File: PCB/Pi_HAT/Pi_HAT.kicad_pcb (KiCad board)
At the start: 2 copper layers, 59 x 65 mm, 15 parts, among them J1 MPU9250, J2 Pi_GPIO, J3 Display, J4 Solenoid I2C, J5 Power Supply

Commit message: Added logo
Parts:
- added G***: LOGO, .pretty:eppl_logo, B.Cu at (137.6, 90.9)
- added G***: LOGO, .pretty:eppl_logo, F.Cu at (103.0, 115.6)
- added H5: MountingHole, MountingHole:MountingHole_2.5mm, F.Cu at (142.9, 109.5)
- added H6: MountingHole, MountingHole:MountingHole_2.5mm, F.Cu at (143.5, 130.0)
- J2: value Pi_GPIO -> PI GPIO
- TB1: value ARDUINO_NANO -> ARDUINO NANO
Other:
- board text added: "12V"
- board text added: "3.3V"
- board text added: "GND"
- board text added: "PI HAT EASY CONTROLS"
- board text added: "SCL"
- board text added: "SDA"
- board text removed: "EPPL"
- board text removed: "Raspberry Pi HAT EASY CONTROLS"

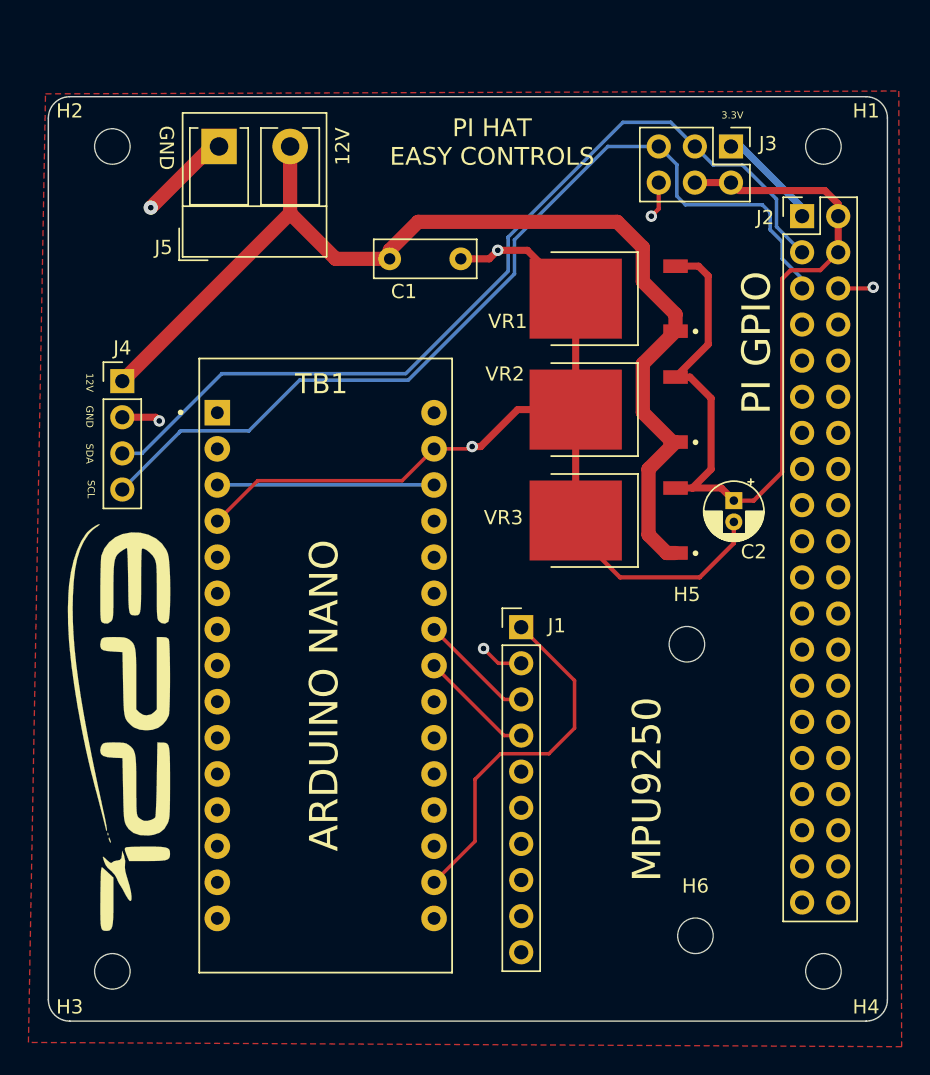
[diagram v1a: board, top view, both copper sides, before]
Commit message: Changed Footprints
Changed the regulator's footprint and added XT-60
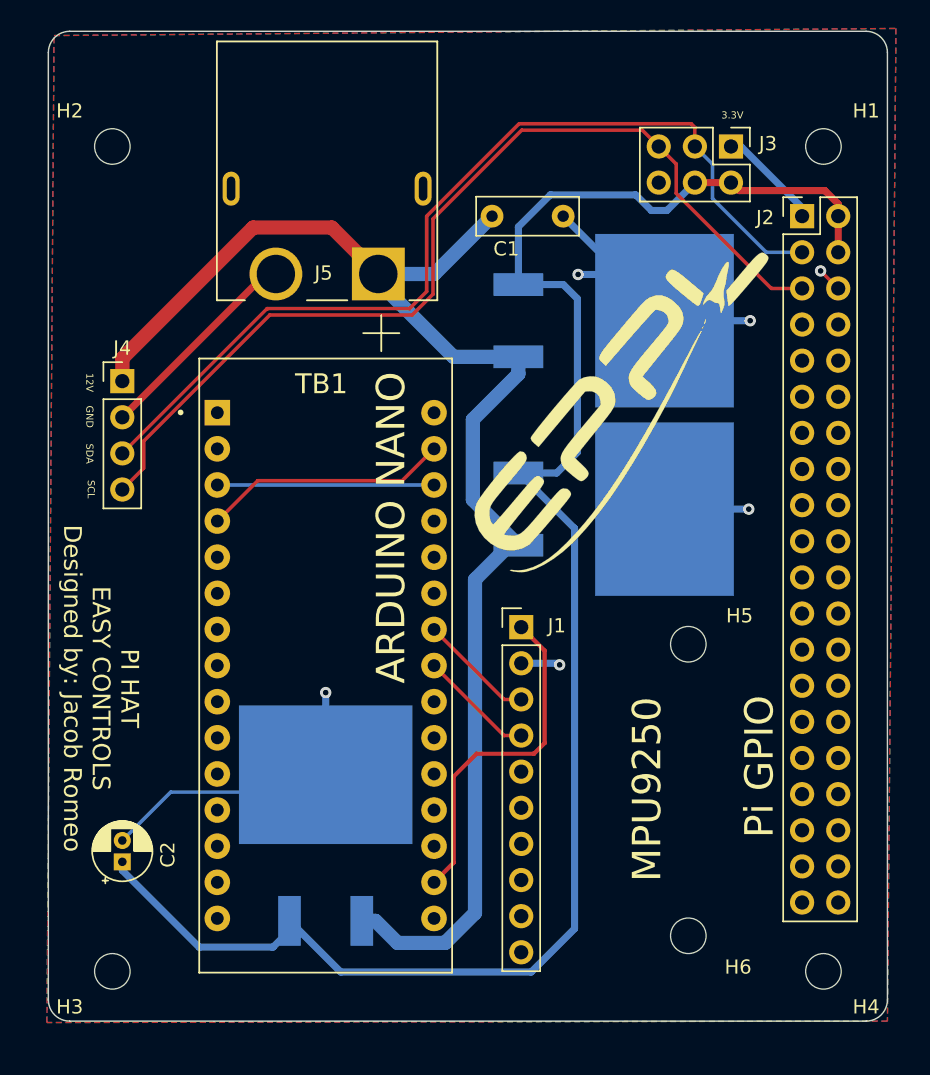
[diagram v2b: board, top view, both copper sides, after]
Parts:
- removed the G*** at (137.6, 90.9)
- removed the G*** at (103.0, 115.6)
- added G***: LOGO, .pretty:eppl_logo, F.Cu at (138.7, 92.3)
- C2: value CP -> C_Polarized
- J2: value PI GPIO -> Pi GPIO
- J5: value Power Supply -> XT60PW-M; footprint TerminalBlock_RND:TerminalBlock_RND_205-00276_1x02_P5.00mm_Vertical -> .pretty:AMASS_XT60PW-M
- VR1, VR2, VR3: value LM78M05CDTX_NOPB -> LM78M05CDTX/NOPB; footprint .pretty:TO228P991X255-3N -> .pretty:VREG_L7805ACD2T; moved to B.Cu
- moved C2 49.9 mm to (103.2, 124.8), turned to 90 degrees
- moved VR3 29.3 mm to (117.5, 122.2), turned to 90 degrees
- moved J5 8.16 mm to (117.6, 77.5)
- moved C1 7.80 mm to (129.2, 79.4)
- moved VR2 7.01 mm to (137.8, 100.0), turned to 0 degrees
- moved VR1 1.59 mm to (137.8, 86.8), turned to 0 degrees
- moved H6 0.50 mm to (143.0, 130.0)
- moved H5 0.10 mm to (143.0, 109.5)
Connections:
- J1 pad 10: Net-(J1-Pad10) -> unconnected-(J1-Pad10)
- J1 pad 5: Net-(J1-Pad5) -> unconnected-(J1-Pad5)
- J1 pad 6: Net-(J1-Pad6) -> unconnected-(J1-Pad6)
- J1 pad 7: Net-(J1-Pad7) -> unconnected-(J1-Pad7)
- J1 pad 8: Net-(J1-Pad8) -> unconnected-(J1-Pad8)
- J1 pad 9: Net-(J1-Pad9) -> unconnected-(J1-Pad9)
- J2 pad 10: Net-(J2-Pad10) -> unconnected-(J2-Pad10)
- J2 pad 11: Net-(J2-Pad11) -> unconnected-(J2-Pad11)
- J2 pad 12: Net-(J2-Pad12) -> unconnected-(J2-Pad12)
- J2 pad 13: Net-(J2-Pad13) -> unconnected-(J2-Pad13)
- J2 pad 14: Net-(J2-Pad14) -> unconnected-(J2-Pad14)
- J2 pad 15: Net-(J2-Pad15) -> unconnected-(J2-Pad15)
- J2 pad 16: Net-(J2-Pad16) -> unconnected-(J2-Pad16)
- J2 pad 17: Net-(J2-Pad17) -> unconnected-(J2-Pad17)
- J2 pad 18: Net-(J2-Pad18) -> unconnected-(J2-Pad18)
- J2 pad 19: Net-(J2-Pad19) -> unconnected-(J2-Pad19)
- J2 pad 20: Net-(J2-Pad20) -> unconnected-(J2-Pad20)
- J2 pad 21: Net-(J2-Pad21) -> unconnected-(J2-Pad21)
- J2 pad 22: Net-(J2-Pad22) -> unconnected-(J2-Pad22)
- J2 pad 23: Net-(J2-Pad23) -> unconnected-(J2-Pad23)
- J2 pad 24: Net-(J2-Pad24) -> unconnected-(J2-Pad24)
- J2 pad 25: Net-(J2-Pad25) -> unconnected-(J2-Pad25)
- J2 pad 26: Net-(J2-Pad26) -> unconnected-(J2-Pad26)
- J2 pad 27: Net-(J2-Pad27) -> unconnected-(J2-Pad27)
- J2 pad 28: Net-(J2-Pad28) -> unconnected-(J2-Pad28)
- J2 pad 29: Net-(J2-Pad29) -> unconnected-(J2-Pad29)
- J2 pad 30: Net-(J2-Pad30) -> unconnected-(J2-Pad30)
- J2 pad 31: Net-(J2-Pad31) -> unconnected-(J2-Pad31)
- J2 pad 32: Net-(J2-Pad32) -> unconnected-(J2-Pad32)
- J2 pad 33: Net-(J2-Pad33) -> unconnected-(J2-Pad33)
- J2 pad 34: Net-(J2-Pad34) -> unconnected-(J2-Pad34)
- J2 pad 35: Net-(J2-Pad35) -> unconnected-(J2-Pad35)
- J2 pad 36: Net-(J2-Pad36) -> unconnected-(J2-Pad36)
- J2 pad 37: Net-(J2-Pad37) -> unconnected-(J2-Pad37)
- J2 pad 38: Net-(J2-Pad38) -> unconnected-(J2-Pad38)
- J2 pad 39: Net-(J2-Pad39) -> unconnected-(J2-Pad39)
- J2 pad 40: Net-(J2-Pad40) -> unconnected-(J2-Pad40)
- J2 pad 7: Net-(J2-Pad7) -> unconnected-(J2-Pad7)
- J2 pad 8: Net-(J2-Pad8) -> unconnected-(J2-Pad8)
- J2 pad 9: Net-(J2-Pad9) -> unconnected-(J2-Pad9)
- J5 pad 1: GND -> 12V
- J5 pad 2: 12V -> GND
- TB1 pad 1: Net-(TB1-Pad1) -> unconnected-(TB1-Pad1)
- TB1 pad 10: Net-(TB1-Pad10) -> unconnected-(TB1-Pad10)
- TB1 pad 11: Net-(TB1-Pad11) -> unconnected-(TB1-Pad11)
- TB1 pad 12: Net-(TB1-Pad12) -> unconnected-(TB1-Pad12)
- TB1 pad 13: Net-(TB1-Pad13) -> unconnected-(TB1-Pad13)
- TB1 pad 14: Net-(TB1-Pad14) -> unconnected-(TB1-Pad14)
- TB1 pad 15: Net-(TB1-Pad15) -> unconnected-(TB1-Pad15)
- TB1 pad 16: Net-(TB1-Pad16) -> unconnected-(TB1-Pad16)
- TB1 pad 18: Net-(TB1-Pad18) -> unconnected-(TB1-Pad18)
- TB1 pad 19: Net-(TB1-Pad19) -> unconnected-(TB1-Pad19)
- TB1 pad 2: Net-(TB1-Pad2) -> unconnected-(TB1-Pad2)
- TB1 pad 20: Net-(TB1-Pad20) -> unconnected-(TB1-Pad20)
- TB1 pad 21: Net-(TB1-Pad21) -> unconnected-(TB1-Pad21)
- TB1 pad 22: Net-(TB1-Pad22) -> unconnected-(TB1-Pad22)
- TB1 pad 25: Net-(TB1-Pad25) -> unconnected-(TB1-Pad25)
- TB1 pad 26: Net-(TB1-Pad26) -> unconnected-(TB1-Pad26)
- TB1 pad 27: Net-(TB1-Pad27) -> unconnected-(TB1-Pad27)
- TB1 pad 28: Net-(TB1-Pad28) -> unconnected-(TB1-Pad28)
- TB1 pad 3: Net-(TB1-Pad28) -> unconnected-(TB1-Pad28)
- TB1 pad 30: Net-(TB1-Pad30) -> unconnected-(TB1-Pad30)
- TB1 pad 5: Net-(TB1-Pad5) -> unconnected-(TB1-Pad5)
- TB1 pad 6: Net-(TB1-Pad6) -> unconnected-(TB1-Pad6)
- TB1 pad 7: Net-(TB1-Pad7) -> unconnected-(TB1-Pad7)
- TB1 pad 8: Net-(TB1-Pad8) -> unconnected-(TB1-Pad8)
- TB1 pad 9: Net-(TB1-Pad9) -> unconnected-(TB1-Pad9)
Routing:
- net /5V: track 61.7 -> 125.2 mm
- net 12V: track 76.1 -> 99.9 mm
- net unconnected-(TB1-Pad28): track 0.00 -> 15.2 mm
- net Net-(TB1-Pad28): track 15.2 -> 0.00 mm
- net /SDA: track 63.8 -> 66.4 mm
- net /SCL: track 66.4 -> 68.3 mm
- net GND: track 87.0 -> 88.5 mm, vias 7 -> 6
- net 3.3VN: track 25.6 -> 24.2 mm
- added copper zone on B.Cu, net GND
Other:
- board size 59 x 65 mm -> 59 x 69.6 mm
- net class Default removed
- board text added: "PI HAT EASY CONTROLS Designed by: Jacob Romeo"
- board text removed: "PI HAT EASY CONTROLS"
